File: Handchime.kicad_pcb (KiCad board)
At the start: 2 copper layers, 40.6 x 16.5 mm, 24 parts, among them J1 USB_C_Receptacle_USB2.0_16P, J2 Pins, J3 SWD, SW0 BOOT, SW1 Row 0, Col 0, SW2 Row 0, Col 1, U1 STM32C071GBUx, U2 PRTR5V0U2X, U3 XC6206P332MR-G

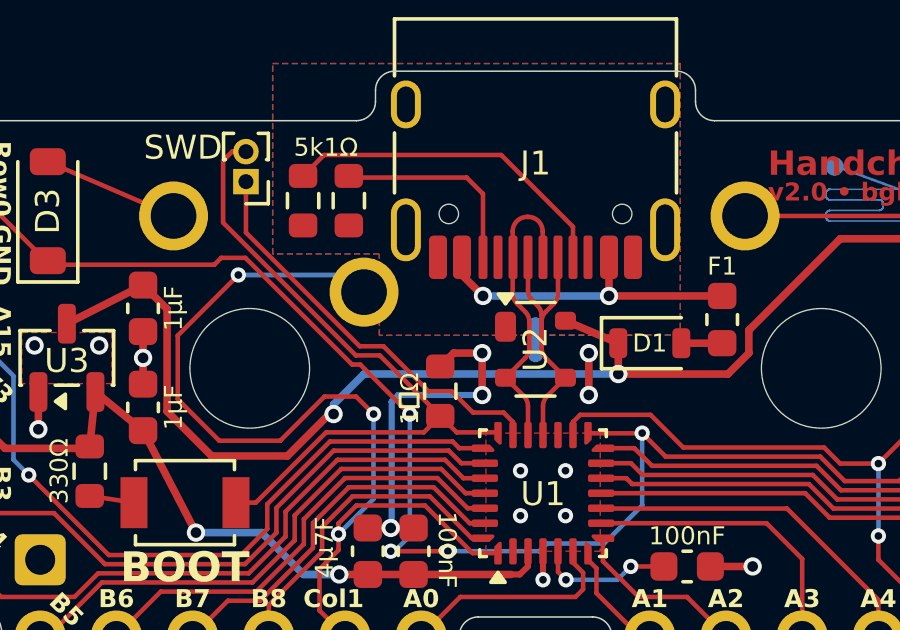
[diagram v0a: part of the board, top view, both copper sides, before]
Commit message: Add pad for shield ground connection to (metal) case
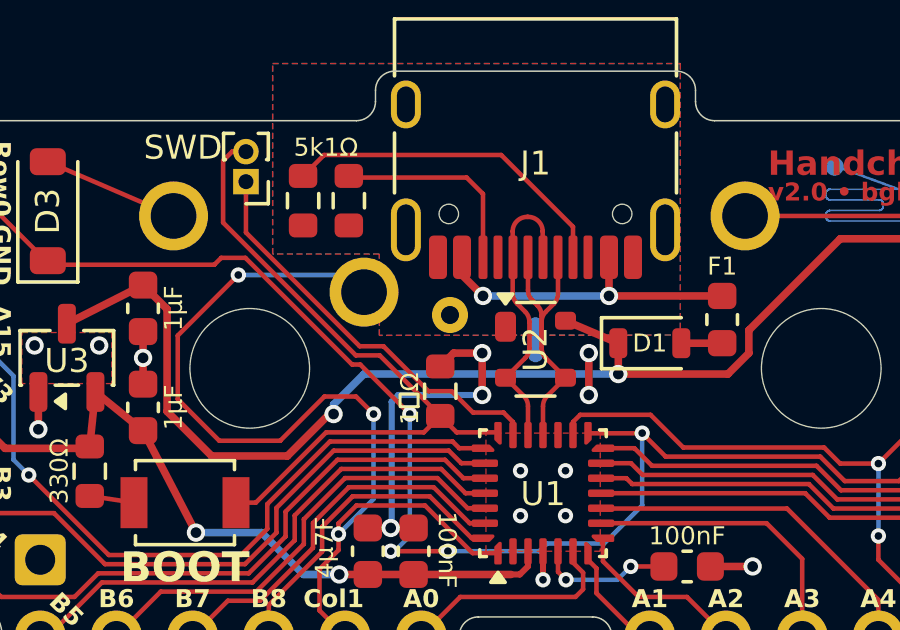
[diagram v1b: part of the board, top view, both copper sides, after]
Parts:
- added J4: Case, Project Library:GroundingPoint, B.Cu at (149.6, 49.0)
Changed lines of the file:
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@@
 		)
+	)
+	(footprint "Project Library:GroundingPoint"
+		(layer "B.Cu")
+		(at 149.606 49.022 180)
+		(descr "Mounting Hole 2.2mm, M2, DIN965")
+		(tags "mounting hole 2.2mm m2 din965")
+		(property "Reference" "J4"
+			(at 0 2.9 0)
+			(layer "B.Fab")
+			(effects
+				(font
+					(size 1 1)
+					(thickness 0.15)
+				)
+				(justify mirror)
+			)
+		)
+		(property "Value" "Case"
+			(at 0 -2.9 0)
+			(layer "B.Fab")
+			(effects
+				(font
+					(size 1 1)
+					(thickness 0.15)
+				)
+				(justify mirror)
+			)
+		)
+		(property "Datasheet" ""
+			(at 0 0 0)
+			(layer "B.Fab")
+			(hide yes)
+			(effects
+				(font
+					(size 1.27 1.27)
+				)
+				(justify mirror)
+			)
+		)
+		(property "Description" ""
+			(at 0 0 0)
+			(layer "B.Fab")
+			(hide yes)
+			(effects
+				(font
+					(size 1.27 1.27)
+				)
+				(justify mirror)
+			)
+		)
+		(property ki_fp_filters "Connector*:*_1x??_*")
+		(sheetname "/")
+		(sheetfile "Handchime.kicad_sch")
+		(zone_connect 2)
+		(attr exclude_from_pos_files exclude_from_bom)
+		(net_tie_pad_groups "1,2")
+		(duplicate_pad_numbers_are_jumpers no)
+		(fp_circle
+			(center 0 0)
+			(end 0.8 0)
+			(stroke
+				(width 0.05)
+				(type solid)
+			)
+			(fill no)
+			(layer "B.CrtYd")
+		)
+		(fp_text user "⏚"
+			(at 0 1.397 180)
+			(unlocked yes)
+			(layer "B.SilkS")
+			(effects
+				(font
+					(size 1 1)
+					(thickness 0.15)
+				)
+			)
+		)
+		(pad "1" thru_hole circle
+			(at 0.056001 0 180)
+			(size 1.2 1.2)
+			(drill 0.6)
+			(layers "*.Cu" "*.Mask")
+			(remove_unused_layers no)
+			(net "ISLAND")
+			(pinfunction "Pin_1_1")
+			(pintype "passive")
+		)
+		(embedded_fonts no)
 	)
 	(gr_poly

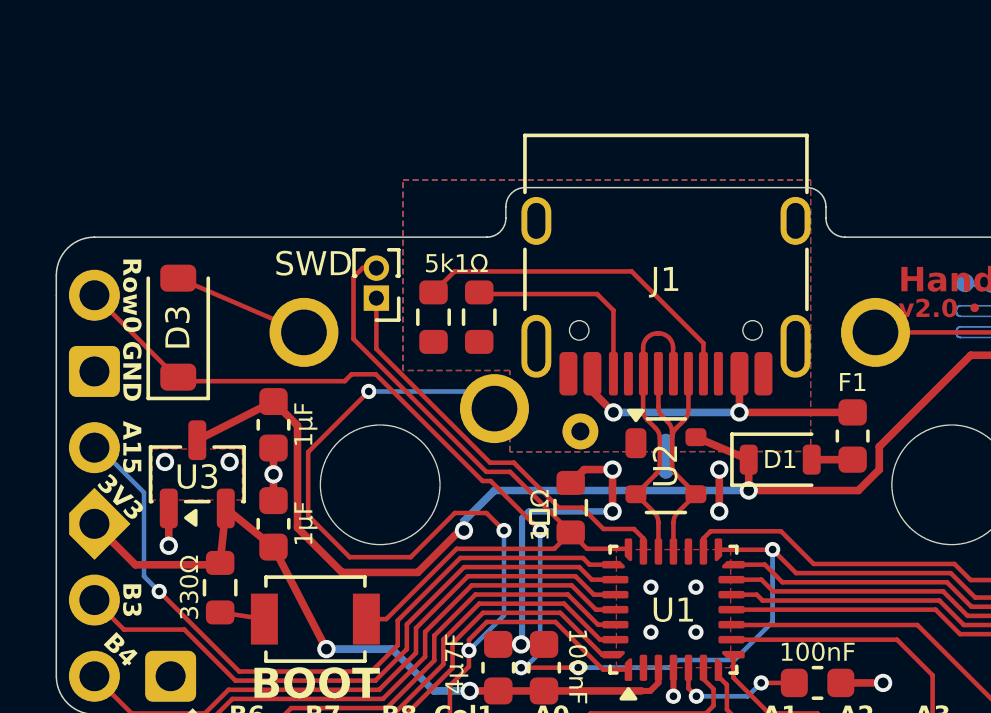
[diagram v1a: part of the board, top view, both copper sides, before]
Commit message: Make grounding connection part of SWD access point
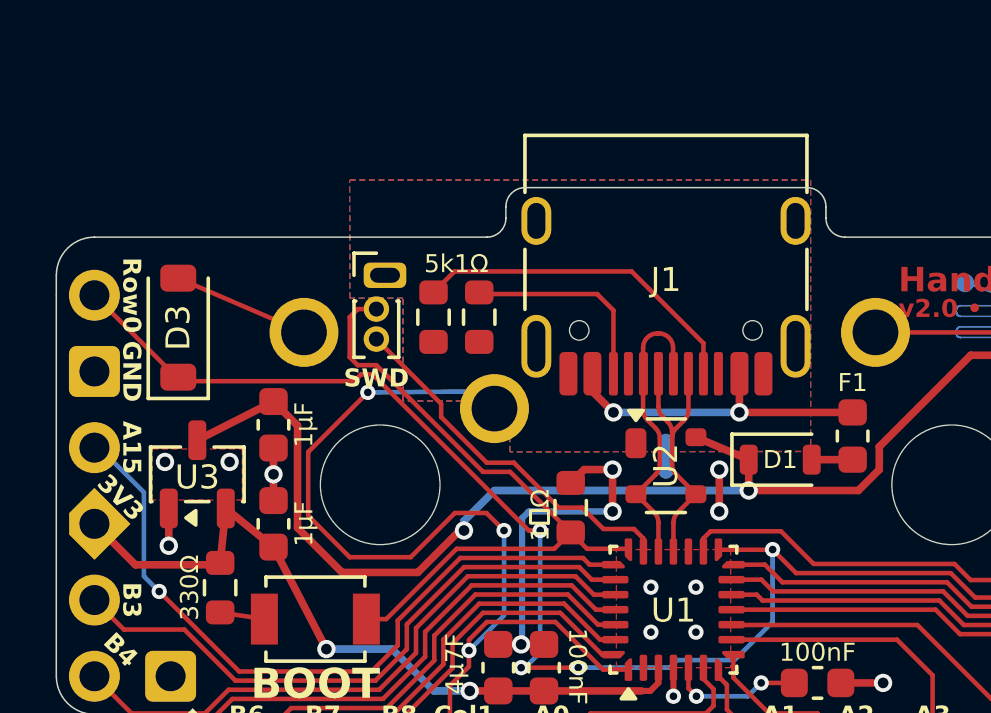
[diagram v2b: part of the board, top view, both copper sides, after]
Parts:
- removed J4: Case, Project Library:GroundingPoint
- J3: footprint Connector_PinHeader_1.00mm:PinHeader_1x02_P1.00mm_Vertical -> Project Library:SWD+GroundingPoint
- moved J3 0.76 mm to (142.7, 43.8), turned to 0 degrees
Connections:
- J3 pad 1: SWDIO -> ISLAND
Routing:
- net SWDIO: track 13.7 -> 12.3 mm
- net BOOT0/SWCLK: track 23.0 -> 22.3 mm

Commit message: Tweak routing
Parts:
- moved R3 1.08 mm to (166.6, 53.6)
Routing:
- net RGB: track 21.0 -> 19.5 mm
- net R0: track 58.7 -> 57.2 mm
- net VCC: track 51.1 -> 50.5 mm

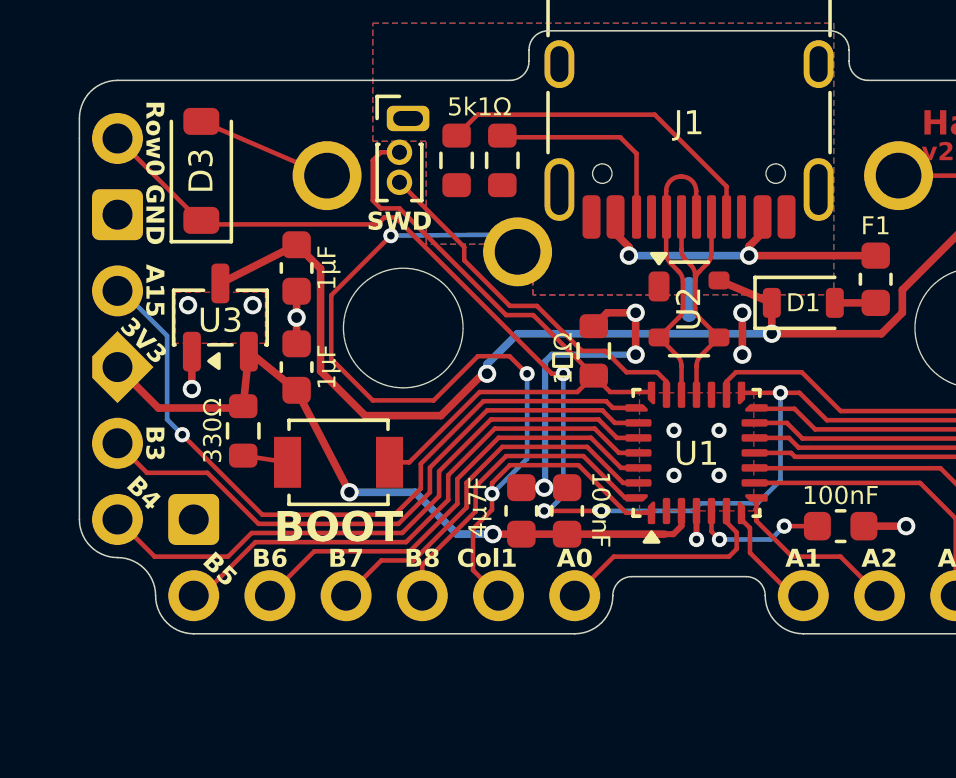
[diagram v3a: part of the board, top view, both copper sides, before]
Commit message: Try to improve routing of Col1 trace
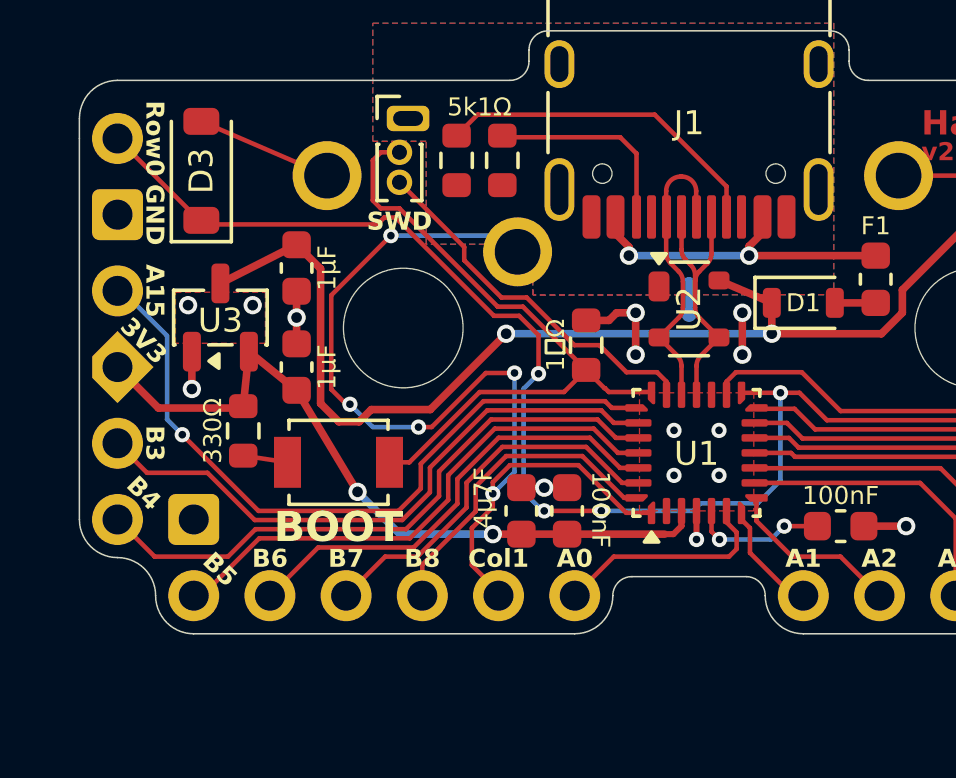
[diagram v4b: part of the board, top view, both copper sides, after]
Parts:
- moved R4 0.32 mm to (149.0, 51.4)
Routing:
- net GND: track 20.0 -> 12.9 mm
- net VCC: track 50.5 -> 51.1 mm
- net C1: track 32.4 -> 32.7 mm, vias 3 -> 5
